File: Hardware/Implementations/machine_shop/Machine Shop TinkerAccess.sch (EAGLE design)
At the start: 41 parts, among them J1 TB_2X1_TE_CONN_ED555_2DS, J10 HDR_4X1_2.54MM_LOCKING_RA, J11 HDR_4X1_2.54MM_LOCKING_RA, J2 TB_2X1_TE_CONN_ED555_2DS, J3 TB_2X1_TE_CONN_ED555_2DS, J4 TB_2X1_TE_CONN_ED555_2DS, J5 TB_2X1_TE_CONN_ED555_2DS, J6 TB_2X1_TE_CONN_ED555_2DS, J7 TB_2X1_TE_CONN_ED555_2DS, J8 HDR_4X1_2.54MM_LOCKING_RA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

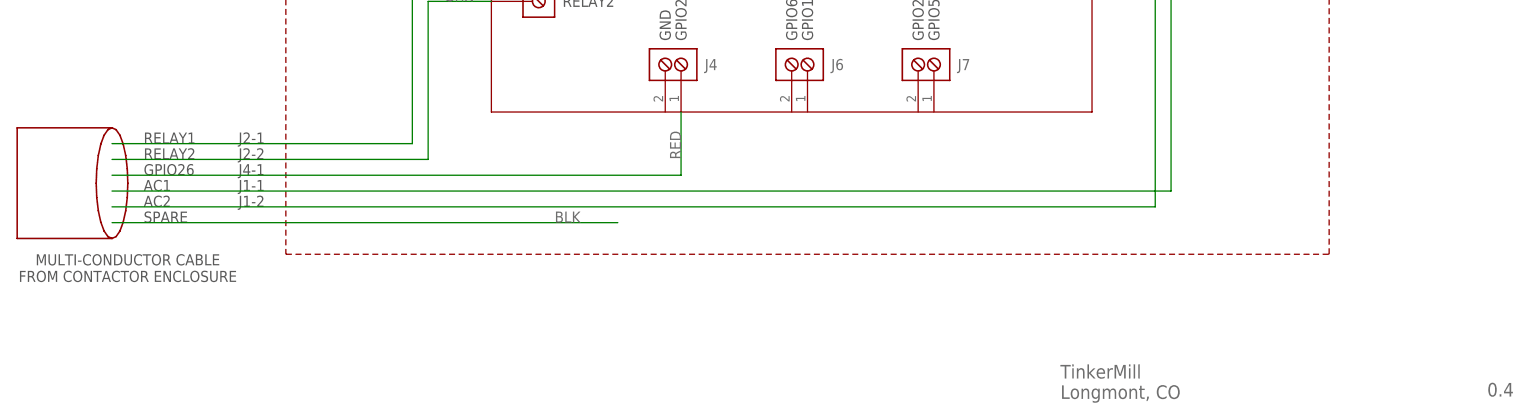
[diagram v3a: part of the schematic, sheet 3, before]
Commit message: Moved E-Stop input to GPIO6 Added machine shop faceplate DXF file
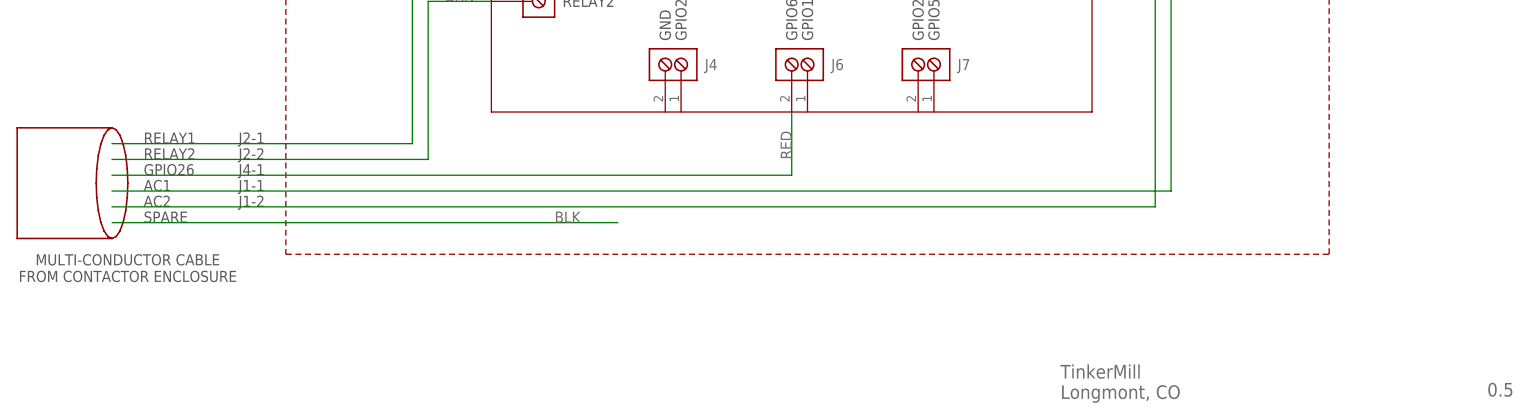
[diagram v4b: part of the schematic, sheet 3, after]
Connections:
- net RED: now also J6.2; no longer J4.1
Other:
- note added: "0.5"
- note added: "NOTES: 1) E-STOP SENSE IS CONNECTED TO RPi GPIO6 SO THAT TINKERACCESS CAN AUTOMATICALLY LOGOUT USER ON AN E-STOP EVENT. THIS ENSURES THAT POWER IS NOT IMMEDIATELY RESTORED WHEN E-STOP IS RESET."
- note removed: "0.4"
- note removed: "NOTES: 1) E-STOP SENSE IS CONNECTED TO RPi GPIO26 SO THAT TINKERACCESS CAN AUTOMATICALLY LOGOUT USER ON AN E-STOP EVENT. THIS ENSURES THAT POWER IS NOT IMMEDIATELY RESTORED WHEN E-STOP IS RESET."
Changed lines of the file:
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@@
 <text x="175.26" y="12.7" size="2.1844" layer="95" align="top-left">TinkerMill
 Longmont, CO</text>
-<text x="243.84" y="7.62" size="2.1844" layer="95">0.4</text>
+<text x="243.84" y="7.62" size="2.1844" layer="95">0.5</text>
 <wire x1="95.25" y1="53.34" x2="113.03" y2="53.34" width="0.254" layer="94"/>
 <wire x1="113.03" y1="53.34" x2="113.03" y2="35.56" width="0.254" layer="94"/>
@@
 <text x="175.26" y="12.7" size="2.1844" layer="95" align="top-left">TinkerMill
 Longmont, CO</text>
-<text x="243.84" y="7.62" size="2.1844" layer="95">0.4</text>
+<text x="243.84" y="7.62" size="2.1844" layer="95">0.5</text>
 <text x="127" y="139.7" size="2.54" layer="97" align="bottom-center">HIGH VOLTAGE CONTACTOR ENCLOSURE</text>
 <wire x1="21.59" y1="86.36" x2="33.02" y2="86.36" width="0.1524" layer="94" style="shortdash"/>
@@
 <text x="193.04" y="170.18" size="2.54" layer="97" align="bottom-center">DISCONNECT</text>
 <text x="15.24" y="182.88" size="1.778" layer="97" align="top-left">NOTES:
-1) E-STOP SENSE IS CONNECTED TO RPi GPIO26 SO THAT TINKERACCESS CAN AUTOMATICALLY LOGOUT USER
+1) E-STOP SENSE IS CONNECTED TO RPi GPIO6 SO THAT TINKERACCESS CAN AUTOMATICALLY LOGOUT USER
      ON AN E-STOP EVENT. THIS ENSURES THAT POWER IS NOT IMMEDIATELY RESTORED WHEN E-STOP IS RESET.</text>
 <text x="240.03" y="53.34" size="1.778" layer="97" align="center">G</text>
@@
 <text x="175.26" y="12.7" size="2.1844" layer="95" align="top-left">TinkerMill
 Longmont, CO</text>
-<text x="243.84" y="7.62" size="2.1844" layer="95">0.4</text>
+<text x="243.84" y="7.62" size="2.1844" layer="95">0.5</text>
 <text x="95.25" y="114.3" size="1.778" layer="97" align="center-left">+5V</text>
 <text x="95.25" y="111.76" size="1.778" layer="97" align="center-left">GND</text>
@@
 <net name="RED" class="0">
 <segment>
-<label x="114.3" y="45.72" size="1.778" layer="95" rot="R90"/>
-<pinref part="J4" gate="G$1" pin="1"/>
-<wire x1="22.86" y1="43.18" x2="114.3" y2="43.18" width="0.1524" layer="91"/>
-<wire x1="114.3" y1="43.18" x2="114.3" y2="53.34" width="0.1524" layer="91"/>
-</segment>
-</net>
+<label x="132.08" y="45.72" size="1.778" layer="95" rot="R90"/>
+<wire x1="22.86" y1="43.18" x2="132.08" y2="43.18" width="0.1524" layer="91"/>
+<pinref part="J6" gate="G$1" pin="2"/>
+<wire x1="132.08" y1="43.18" x2="132.08" y2="53.34" width="0.1524" layer="91"/>
+</segment>
+</net>

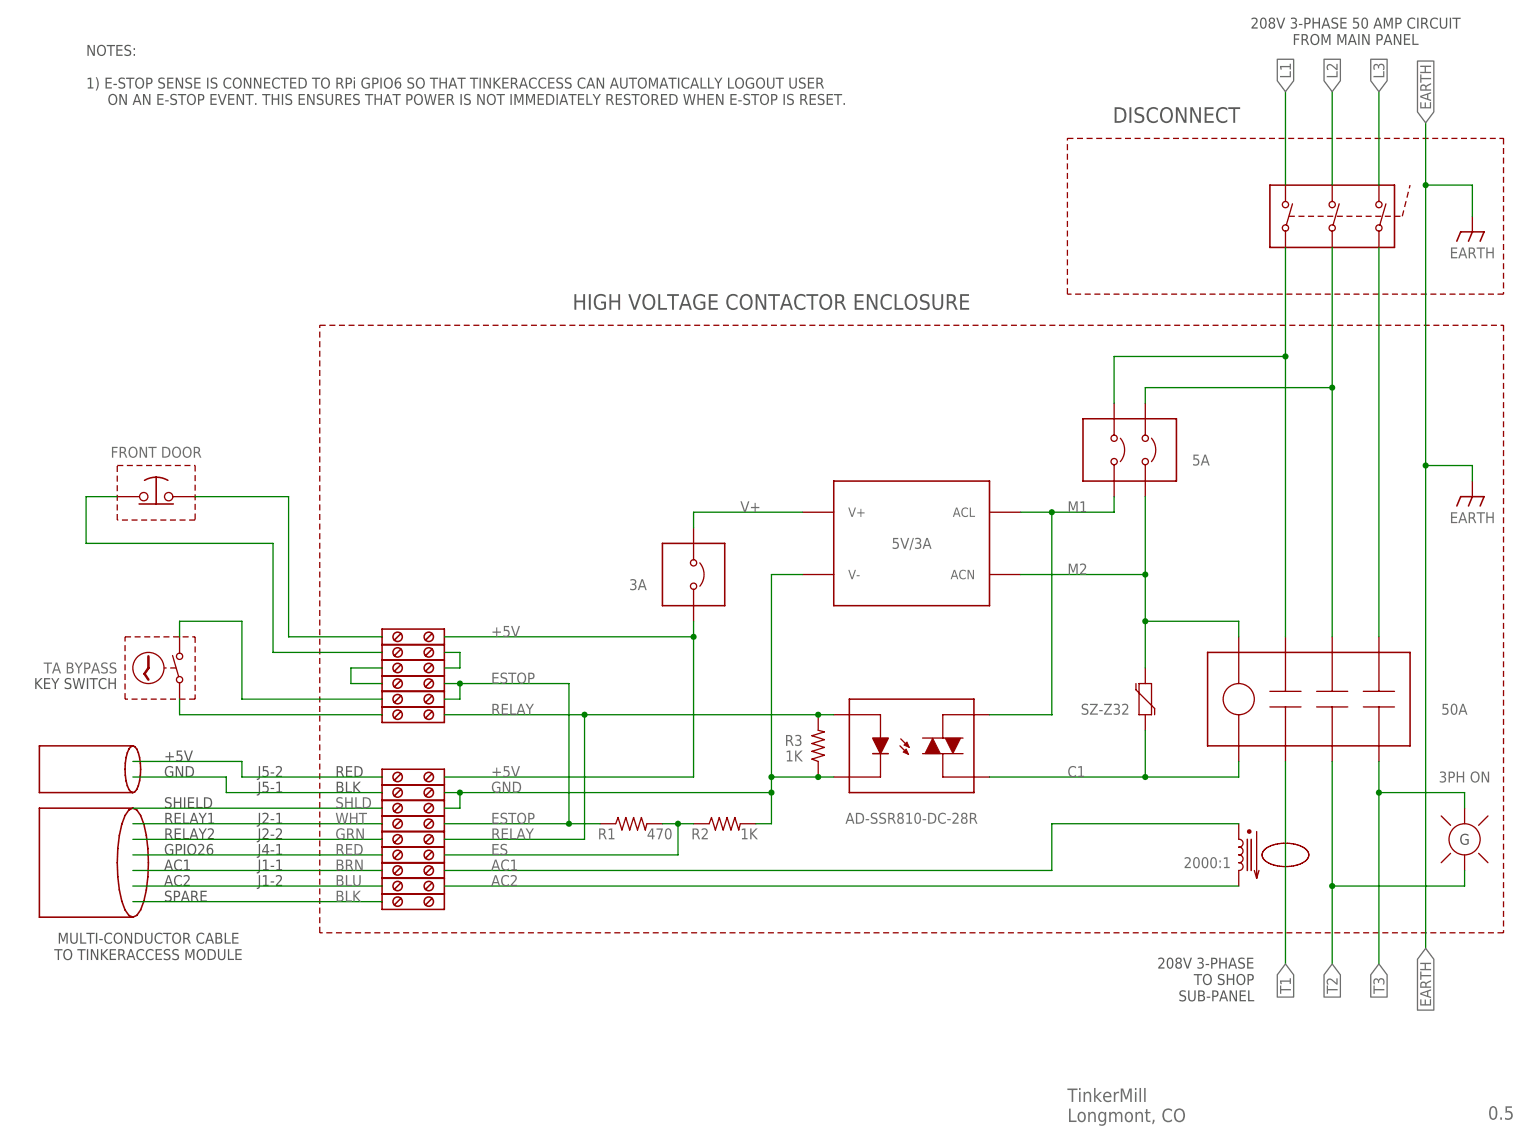
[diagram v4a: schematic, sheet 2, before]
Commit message: Updated machine shop schematic with bypass detect changes
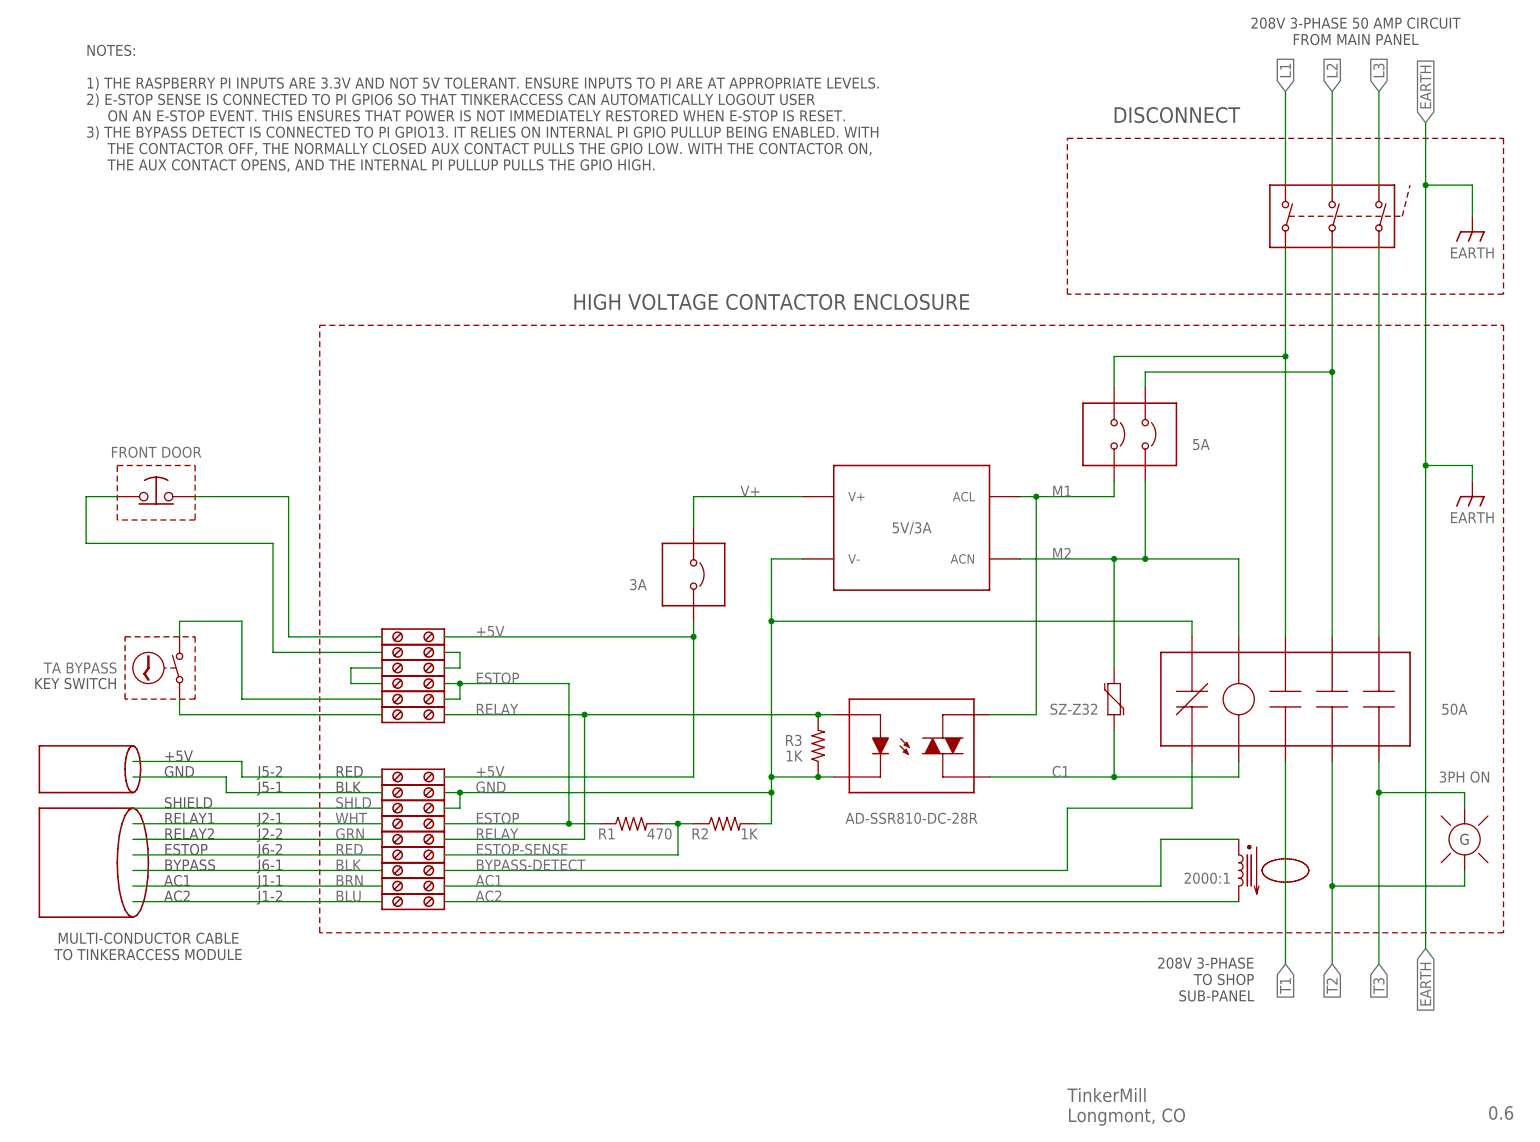
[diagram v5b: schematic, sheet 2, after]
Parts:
- K1: device TMF_Schematic_Only:CONTACTOR_3POLE -> TMF_Schematic_Only:CONTACTOR_3POLE_NC_AUX
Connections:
- net ES renamed ESTOP-SENSE
- new net BYPASS-DETECT: K1.NC2, TB9.B
- net AC1: now also TB10.B; no longer TB9.B
- net AC2: now also TB4.B; no longer TB10.B
- net BLK: now also J6.1
- net GND: now also K1.NC1
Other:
- note added: "0.6"
- note added: "BYPASS"
- note added: "J6-1"
- note added: "J6-2"
- note added: "NOTES: 1) THE RASPBERRY PI INPUTS ARE 3.3V AND NOT 5V TOLERANT. ENSURE INPUTS TO PI ARE AT APPROPRIATE LEVELS. 2) E-STOP SENSE IS CONNECTED TO PI GPIO6 SO THAT TINKERACCESS CAN AUTOMATICALLY LOGOUT USER ON AN E-STOP EVENT. THIS ENSURES THAT POWER IS NOT IMMEDIATELY RESTORED WHEN E-STOP IS RESET. 3) THE BYPASS DETECT IS CONNECTED TO PI GPIO13. IT RELIES ON INTERNAL PI GPIO PULLUP BEING ENABLED. WI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"
- note removed: "0.5"
- note removed: "J4-1"
- note removed: "NOTES: 1) E-STOP SENSE IS CONNECTED TO RPi GPIO6 SO THAT TINKERACCESS CAN AUTOMATICALLY LOGOUT USER ON AN E-STOP EVENT. THIS ENSURES THAT POWER IS NOT IMMEDIATELY RESTORED WHEN E-STOP IS RESET."
- note removed: "SPARE"

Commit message: Added alarm beacon wiring to machine shop TinkerAccess schematic
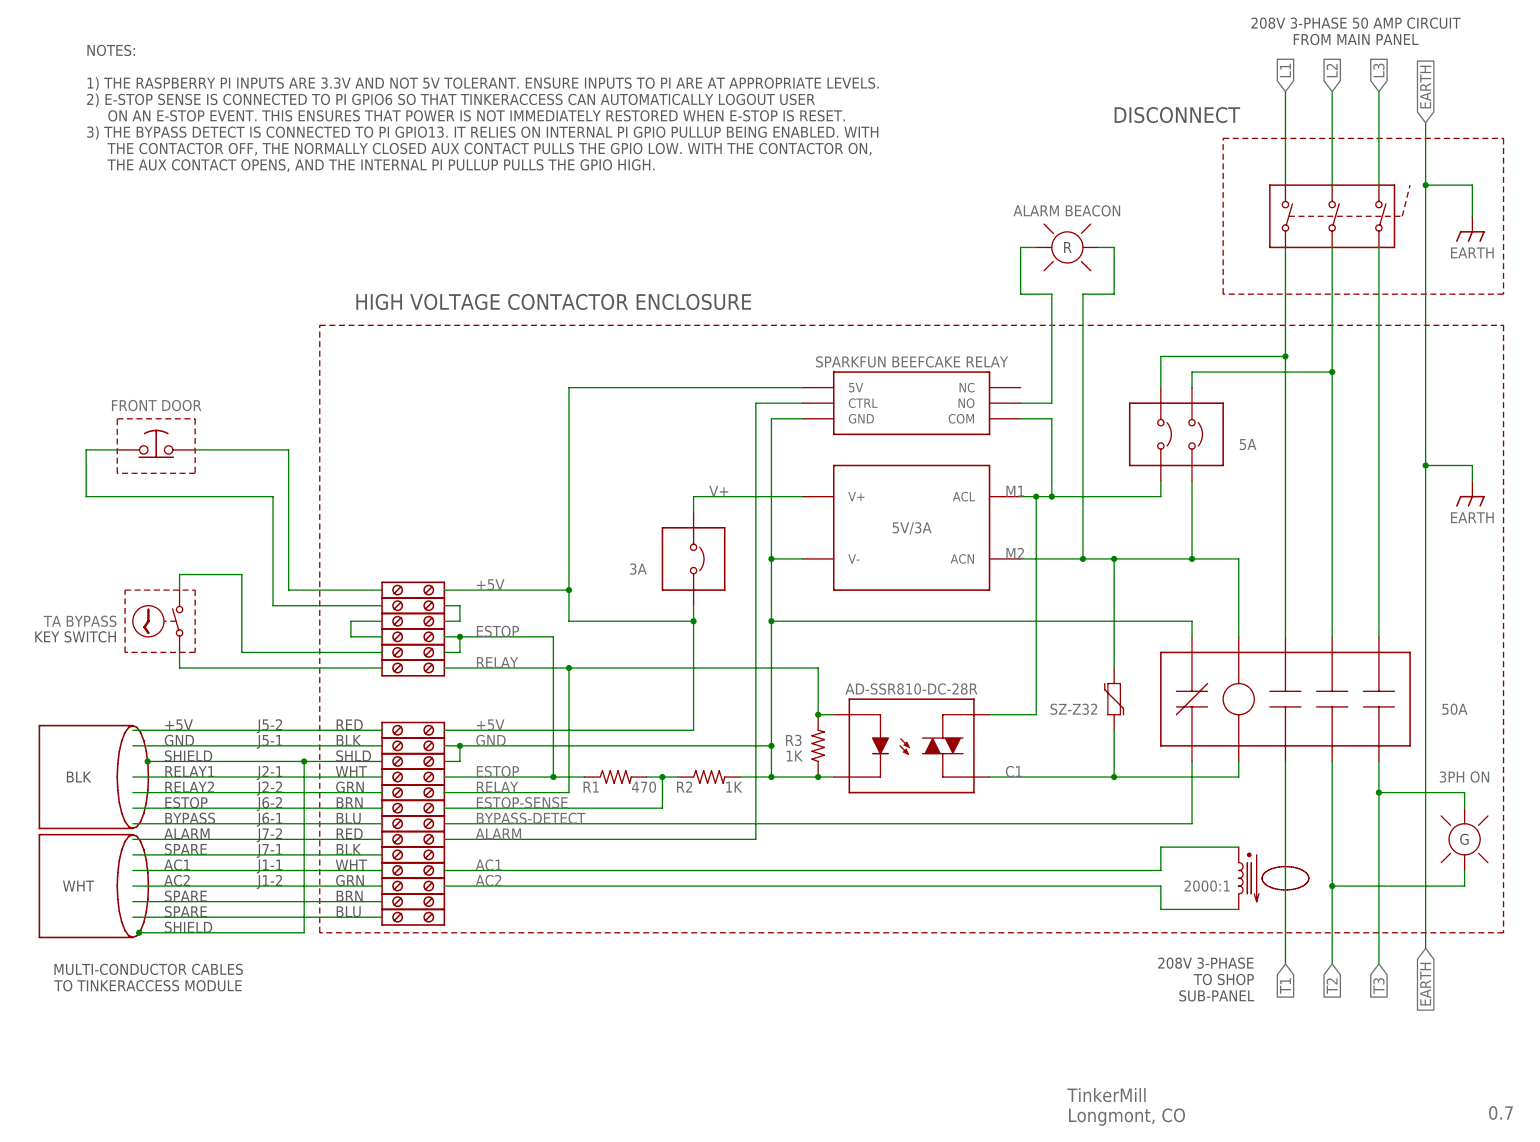
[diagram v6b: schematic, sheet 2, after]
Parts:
- added BD1: SPARKFUN BEEFCAKE RELAY, TMF_Schematic_Only:SPARKFUN_BEEFCAKE
- added LP2: ALARM BEACON, TMF_Schematic_Only:INDICATOR_LAMP
- added TB11, TB12, TB15, TB8: TERMINAL_BLOCK, TMF_Schematic_Only:TERMINAL_BLOCK
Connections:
- net BLU renamed WHT2
- net GRN renamed GRN1
- net RED renamed BRN1
- net WHT renamed WHT1
- net ZBLK renamed BLK1
- net ZRED renamed RED1
- removed net BLK: J6.1, TB4.A
- removed net BRN: J1.1, TB9.A
- new net ALARM: BD1.CTRL, TB8.B
- new net BLK2: J7.1, TB11.A
- new net BLU1: J6.1, TB9.A
- new net BLU2: TB15.A
- new net BRN2: TB12.A
- new net GRN2: J1.1, TB4.A
- new net N$2: BD1.NO, LP2.1
- new net RED2: J7.2, TB8.A
- net +5V: now also BD1.5V
- net GND: now also BD1.GND
- net M1: now also BD1.COM
- net M2: now also LP2.2
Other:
- note added: "0.7"
- note added: "ALARM"
- note added: "BRN"
- note added: "GRN"
- note added: "J7-1"
- note added: "J7-2"
- note added: "MULTI-CONDUCTOR CABLES FROM CONTACTOR ENCLOSURE"
- note added: "MULTI-CONDUCTOR CABLES TO TINKERACCESS MODULE"
- note added: "R"
- note added: "SHLD"
- note added: "SPARE"
- note added: "WHT"
- note removed: "0.6"
- note removed: "MULTI-CONDUCTOR CABLE FROM CONTACTOR ENCLOSURE"
- note removed: "MULTI-CONDUCTOR CABLE TO TINKERACCESS MODULE"
- moved on the sheet: J1, J2, J3, J4, J5, J6, J7, J8, J9, R1, R2

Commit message: Updated final front door and machine shop schematics, BOM, and config files
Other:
- note added: "1.0"
- note removed: "0.7"
- moved on the sheet: J1, J3, J8, J9
